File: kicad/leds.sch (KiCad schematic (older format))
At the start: 85 parts, among them U6 74HC154

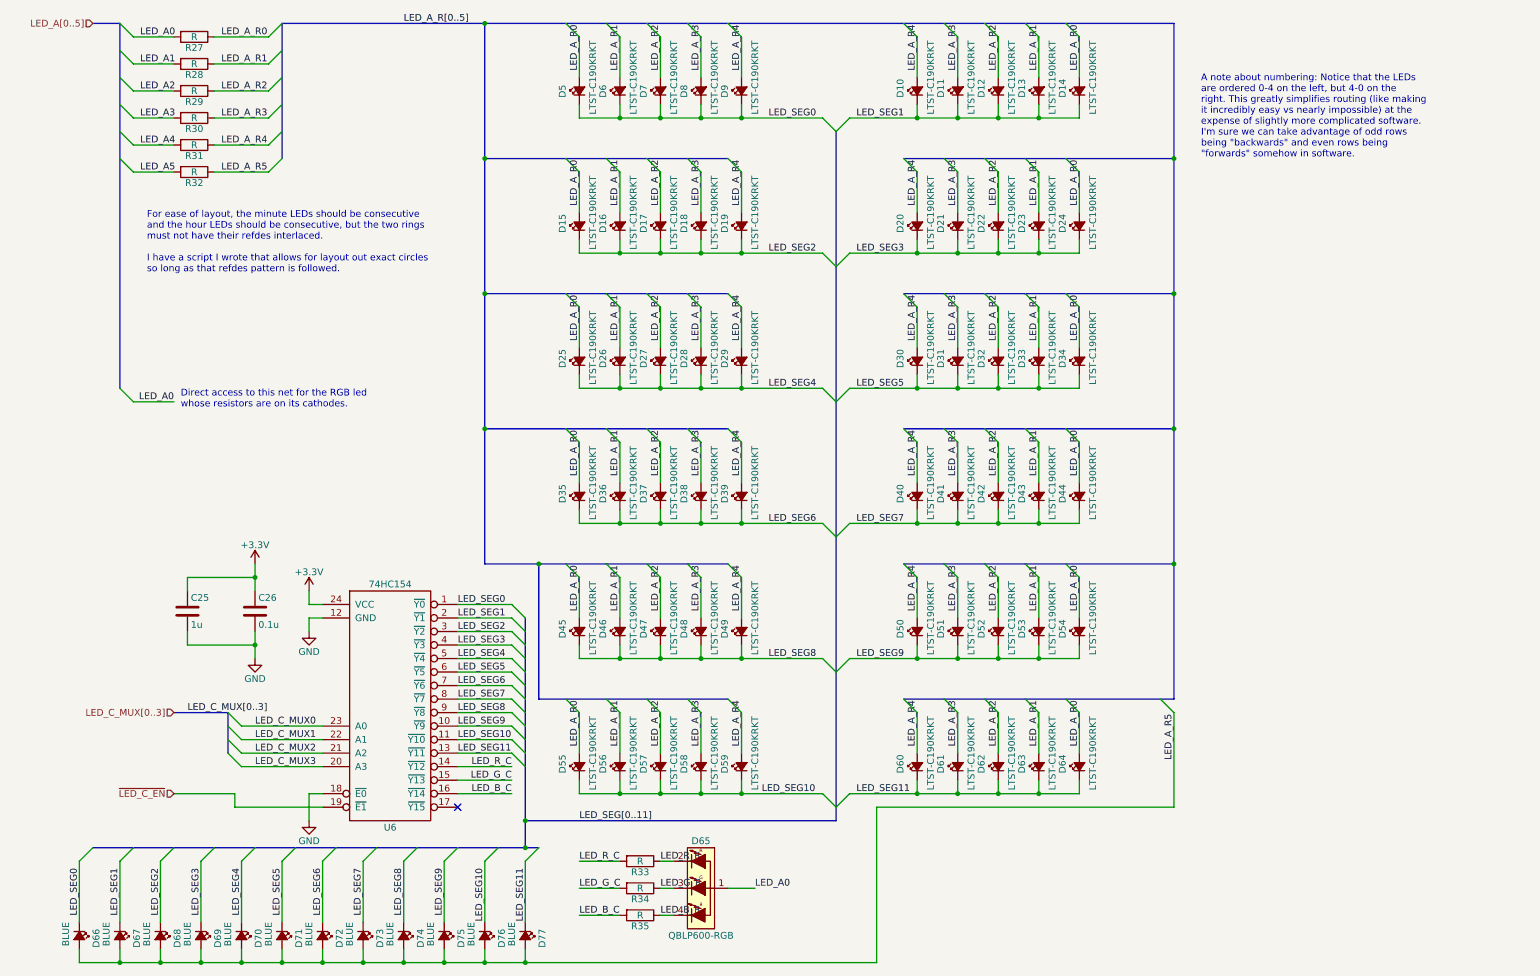
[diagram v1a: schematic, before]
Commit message: Checked layout and reference designs, swapped crystal and RGB LED
ST has a list of suggested crystals which are known to work with the
STM32L0 family. I selected one of those and it is significantly
smaller in all dimensions.

The RGB LED had too high of a green voltage. I swapped it out for a
slightly more expensive one with the same footprint that had startlingly
low green and blue forward voltages.

For layout changes:
- Fixed regulator footprint silkscreen
- Fixed regulator layout to be closer to reference design
- Fixed inductor silkscreen
- Moved accelerometer downward to accomodate capacitors above
- Fixed accelerometer layout to have no traces beneath
- Fixed accelerometer silkscreen
- Fixed LED silkscreen
- General small silkscreen edits, such as shifting text around

I've also chosen parts and values for all resistors and capacitors.
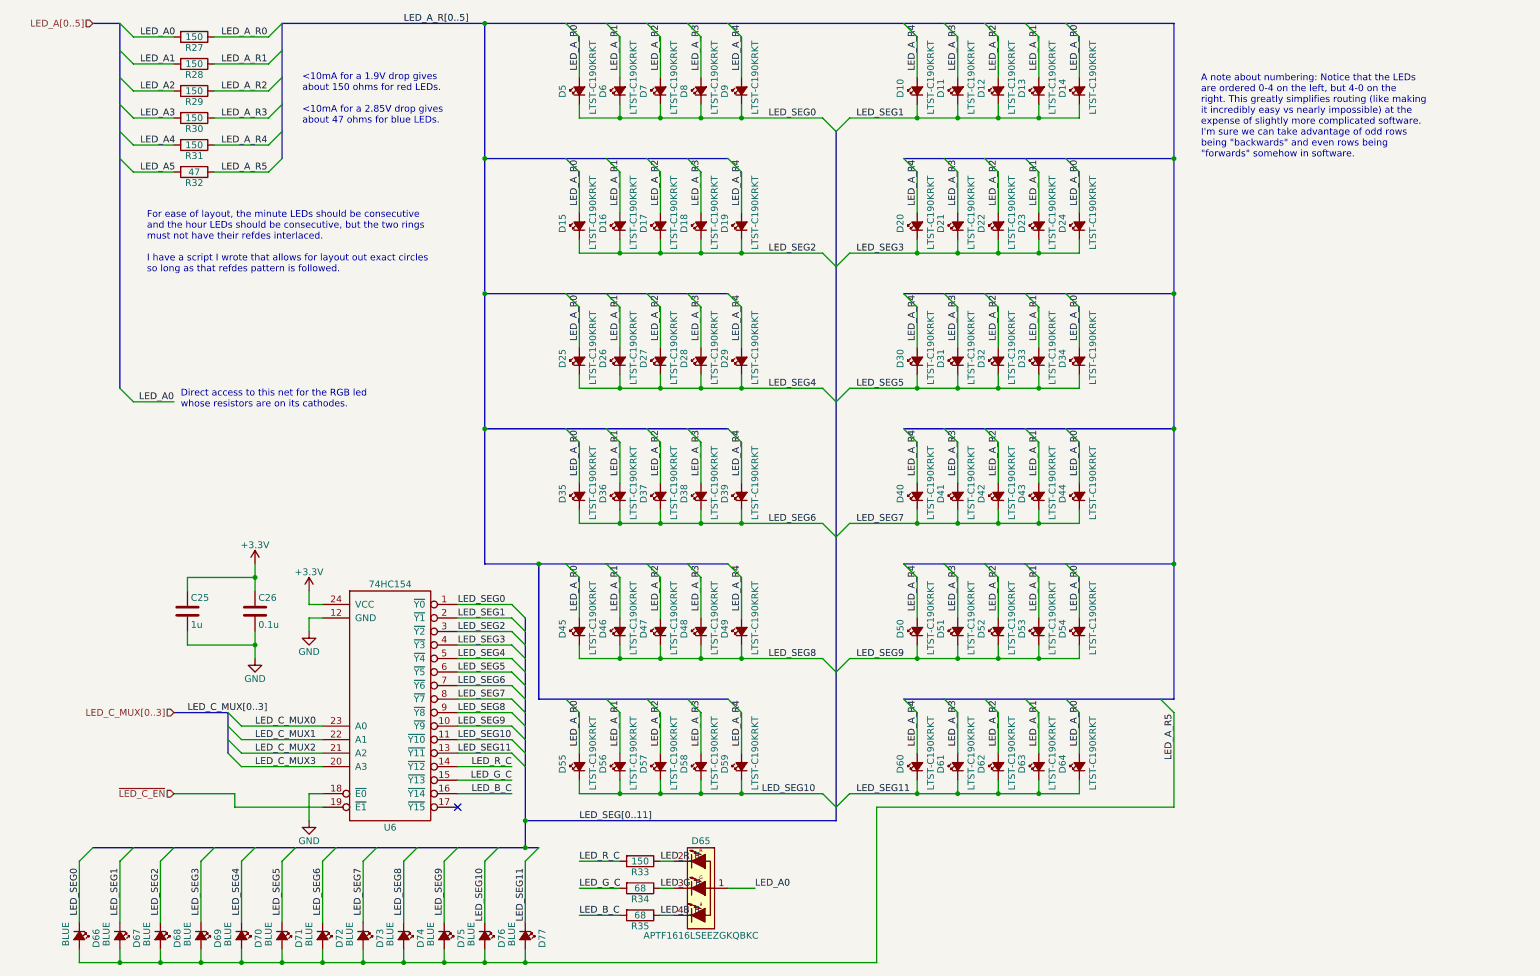
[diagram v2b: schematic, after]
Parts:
- D65: value QBLP600-RGB -> APTF1616LSEEZGKQBKC; Part No. 1516-1184-1-ND -> 754-1972-1-ND
- R27, R28, R29, R30, R31, R33: value R -> 150; Part No. (none) -> 311-150LRCT-ND
- R32: value R -> 47; Part No. (none) -> 311-47.0LRCT-ND
- R34, R35: value R -> 68; Part No. (none) -> 311-68.0LRCT-ND
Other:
- note added: "<10mA for a 1.9V drop gives\nabout 150 ohms for red LEDs.\n\n<10mA for a 2.85V drop gives\nabout 47 ohms for blue LEDs."
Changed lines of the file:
@@
 P 1750 800
 F 0 "R27" V 1830 800 50  0000 C CNN
-F 1 "R" V 1750 800 50  0000 C CNN
+F 1 "150" V 1750 800 50  0000 C CNN
 F 2 "Resistors_SMD:R_0402" V 1680 800 50  0001 C CNN
 F 3 "" H 1750 800 50  0000 C CNN
+F 4 "311-150LRCT-ND" H 1750 800 60  0001 C CNN "Part No."
 	1    1750 800
 	0    1    1    0
@@
 P 1750 1000
 F 0 "R28" V 1830 1000 50  0000 C CNN
-F 1 "R" V 1750 1000 50  0000 C CNN
+F 1 "150" V 1750 1000 50  0000 C CNN
 F 2 "Resistors_SMD:R_0402" V 1680 1000 50  0001 C CNN
 F 3 "" H 1750 1000 50  0000 C CNN
+F 4 "311-150LRCT-ND" H 1750 1000 60  0001 C CNN "Part No."
 	1    1750 1000
 	0    1    1    0
@@
 P 1750 1200
 F 0 "R29" V 1830 1200 50  0000 C CNN
-F 1 "R" V 1750 1200 50  0000 C CNN
+F 1 "150" V 1750 1200 50  0000 C CNN
 F 2 "Resistors_SMD:R_0402" V 1680 1200 50  0001 C CNN
 F 3 "" H 1750 1200 50  0000 C CNN
+F 4 "311-150LRCT-ND" H 1750 1200 60  0001 C CNN "Part No."
 	1    1750 1200
 	0    1    1    0
@@
 P 1750 1400
 F 0 "R30" V 1830 1400 50  0000 C CNN
-F 1 "R" V 1750 1400 50  0000 C CNN
+F 1 "150" V 1750 1400 50  0000 C CNN
 F 2 "Resistors_SMD:R_0402" V 1680 1400 50  0001 C CNN
 F 3 "" H 1750 1400 50  0000 C CNN
+F 4 "311-150LRCT-ND" H 1750 1400 60  0001 C CNN "Part No."
 	1    1750 1400
 	0    1    1    0
@@
 P 1750 1600
 F 0 "R31" V 1830 1600 50  0000 C CNN
-F 1 "R" V 1750 1600 50  0000 C CNN
+F 1 "150" V 1750 1600 50  0000 C CNN
 F 2 "Resistors_SMD:R_0402" V 1680 1600 50  0001 C CNN
 F 3 "" H 1750 1600 50  0000 C CNN
+F 4 "311-150LRCT-ND" H 1750 1600 60  0001 C CNN "Part No."
 	1    1750 1600
 	0    1    1    0
@@
 P 1750 1800
 F 0 "R32" V 1830 1800 50  0000 C CNN
-F 1 "R" V 1750 1800 50  0000 C CNN
+F 1 "47" V 1750 1800 50  0000 C CNN
 F 2 "Resistors_SMD:R_0402" V 1680 1800 50  0001 C CNN
 F 3 "" H 1750 1800 50  0000 C CNN
+F 4 "311-47.0LRCT-ND" H 1750 1800 60  0001 C CNN "Part No."
 	1    1750 1800
 	0    1    1    0
@@
 P 5050 6900
 F 0 "R33" V 5130 6900 50  0000 C CNN
-F 1 "R" V 5050 6900 50  0000 C CNN
+F 1 "150" V 5050 6900 50  0000 C CNN
 F 2 "Resistors_SMD:R_0402" V 4980 6900 50  0001 C CNN
 F 3 "" H 5050 6900 50  0000 C CNN
+F 4 "311-150LRCT-ND" H 5050 6900 60  0001 C CNN "Part No."
 	1    5050 6900
 	0    1    1    0
@@
 P 5050 7100
 F 0 "R34" V 5130 7100 50  0000 C CNN
-F 1 "R" V 5050 7100 50  0000 C CNN
+F 1 "68" V 5050 7100 50  0000 C CNN
 F 2 "Resistors_SMD:R_0402" V 4980 7100 50  0001 C CNN
 F 3 "" H 5050 7100 50  0000 C CNN
+F 4 "311-68.0LRCT-ND" H 5050 7100 60  0001 C CNN "Part No."
 	1    5050 7100
 	0    1    1    0
@@
 P 5050 7300
 F 0 "R35" V 5130 7300 50  0000 C CNN
-F 1 "R" V 5050 7300 50  0000 C CNN
+F 1 "68" V 5050 7300 50  0000 C CNN
 F 2 "Resistors_SMD:R_0402" V 4980 7300 50  0001 C CNN
 F 3 "" H 5050 7300 50  0000 C CNN
+F 4 "311-68.0LRCT-ND" H 5050 7300 60  0001 C CNN "Part No."
 	1    5050 7300
 	0    1    1    0
@@
 P 5500 7100
 F 0 "D65" H 5500 7450 50  0000 C CNN
-F 1 "QBLP600-RGB" H 5500 6750 50  0000 C CNN
+F 1 "APTF1616LSEEZGKQBKC" H 5500 6750 50  0000 C CNN
 F 2 "simple-led-watch:LED-0606" H 5455 7050 50  0001 C CNN
 F 3 "" H 5455 7050 50  0000 C CNN
-F 4 "1516-1184-1-ND" H 5500 7100 60  0001 C CNN "Part No."
+F 4 "754-1972-1-ND" H 5500 7100 60  0001 C CNN "Part No."
 	1    5500 7100
 	1    0    0    -1
@@
 Text Label 5200 7300 0    50   ~ 0
 LED_B_R
+Text Notes 2550 1450 0    50   ~ 0
+<10mA for a 1.9V drop gives\nabout 150 ohms for red LEDs.\n\n<10mA for a 2.85V drop gives\nabout 47 ohms for blue LEDs.
 $EndSCHEMATC
